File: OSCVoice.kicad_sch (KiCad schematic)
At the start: 38 parts, among them U10 TL074, U9 SSI2131

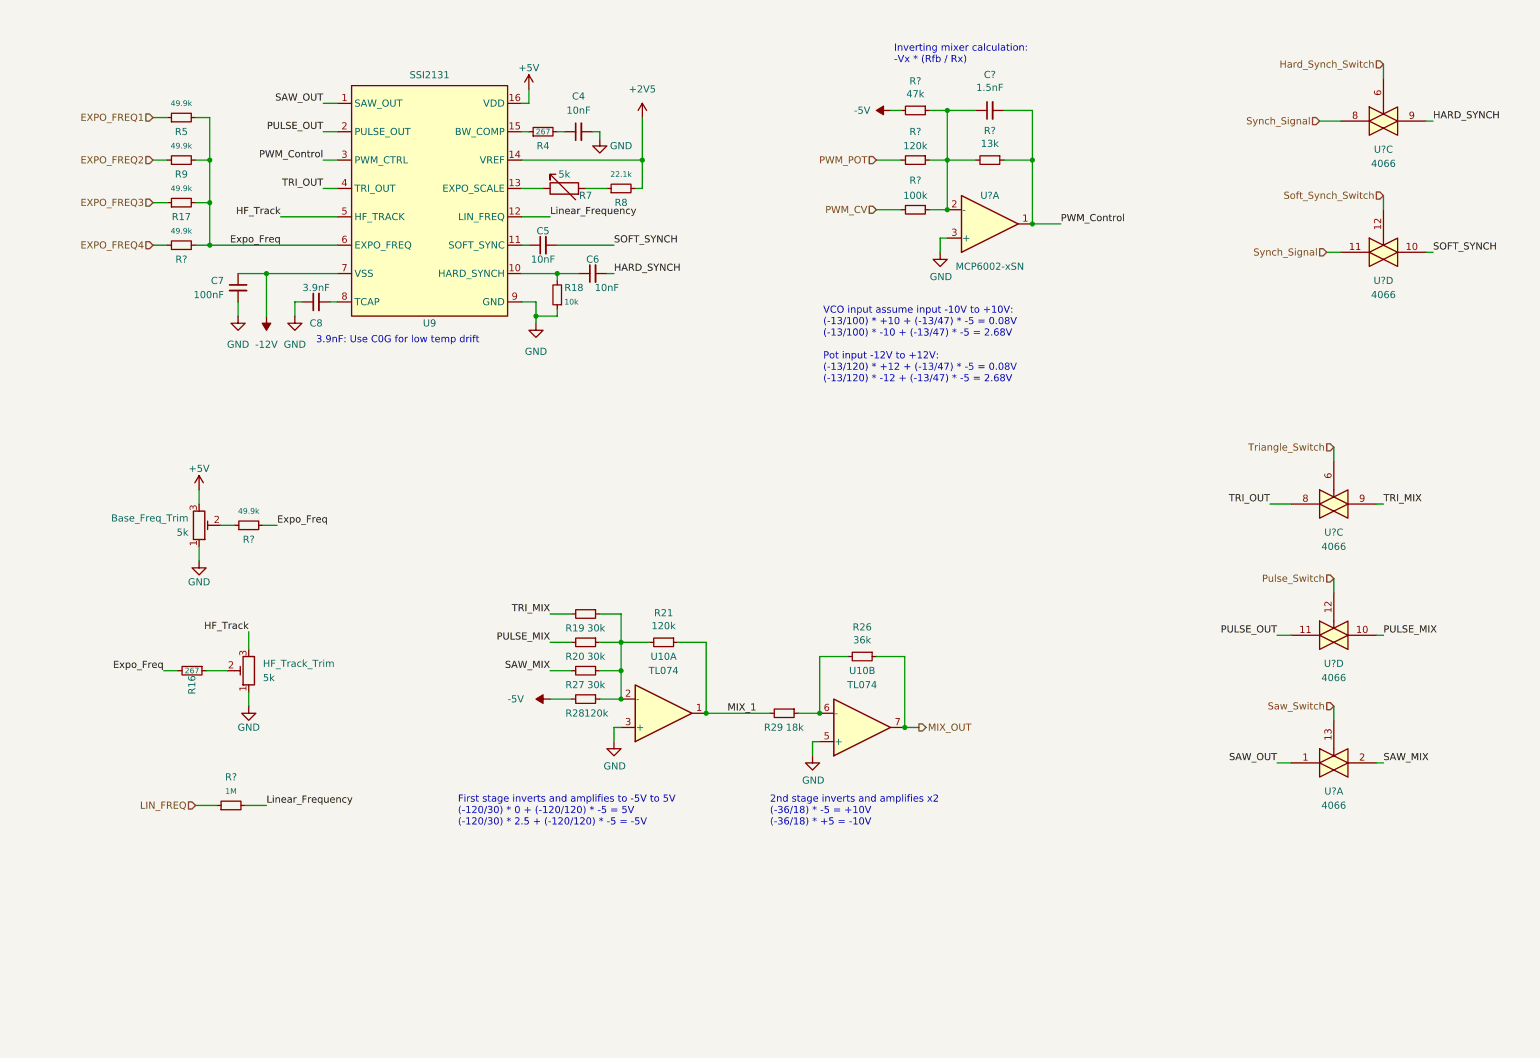
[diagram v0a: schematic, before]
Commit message: Split components and control pcbs
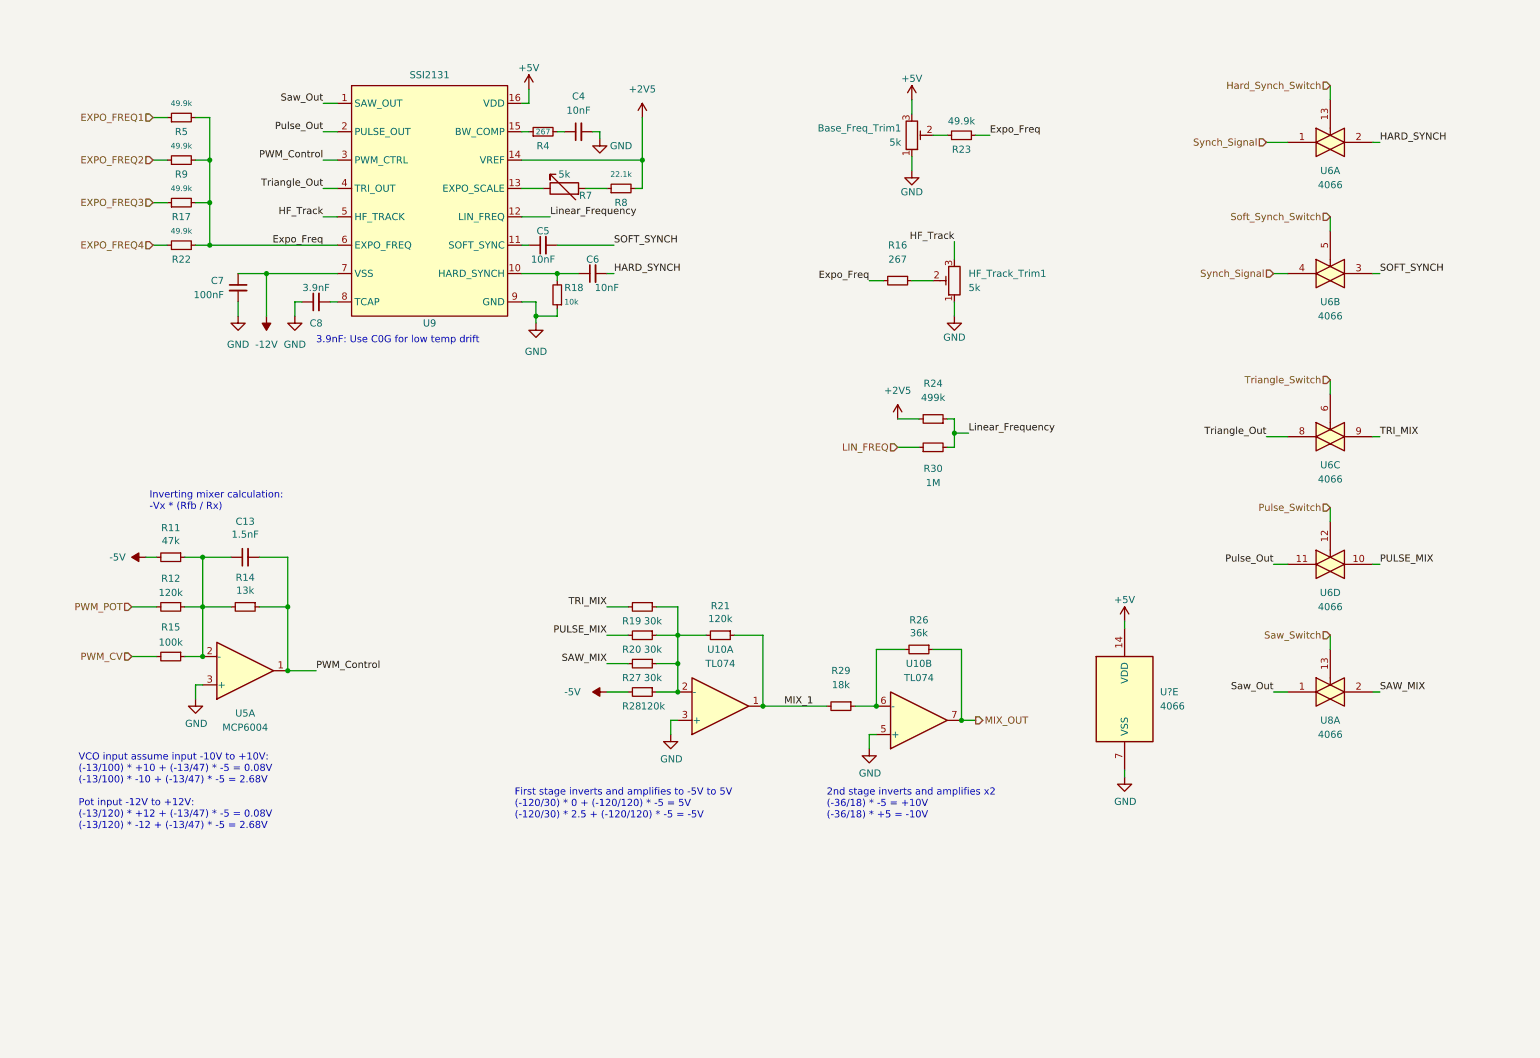
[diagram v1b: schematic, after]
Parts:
- removed U?: MCP6002-xSN, Package_SO:MSOP-8_3x3mm_P0.65mm, symbol Amplifier_Operational:MCP6002-xSN
- added R24: 499k, Resistor_SMD:R_0603_1608Metric, symbol Device:R_Small
- added U5: MCP6004, Package_SO:SOIC-14_3.9x8.7mm_P1.27mm, symbol Amplifier_Operational:MCP6004
- added U?: 4066, Package_SO:TSSOP-14_4.4x5mm_P0.65mm, symbol 4xxx:4066
- C4, C5, C6, C7: footprint Capacitor_SMD:C_0805_2012Metric -> Capacitor_SMD:C_0603_1608Metric_Pad1.08x0.95mm_HandSolder
- R11, R12, R14, R15, R22, R23, R30: renamed from R?; footprint Resistor_SMD:R_0805_2012Metric -> Resistor_SMD:R_0603_1608Metric
- R16, R17, R18, R19, R20, R21, R26, R27, R28, R29, R4, R5, R8, R9: footprint Resistor_SMD:R_0805_2012Metric -> Resistor_SMD:R_0603_1608Metric
- U10: footprint (none) -> Package_SO:SOIC-14_3.9x8.7mm_P1.27mm
- gave numbers to parts that had none: 3
- renumbered Base_Freq_Trim to Base_Freq_Trim1, HF_Track_Trim to HF_Track_Trim1
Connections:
- net +2V5: now also R24.2
- net +5V: now also U?.14 (VDD)
- net GND: now also U5.3 (+), U?.7 (VSS)
- net HARD_SYNCH: now also U6.2; no longer U6.9
- net Hard_Synch_Switch: now also U6.13; no longer U6.6
- net Linear_Frequency: now also R24.1
- net PWM_Control: now also U5.1
- net SOFT_SYNCH: now also U6.3; no longer U6.10
- net Soft_Synch_Switch: now also U6.5; no longer U6.12
- net Synch_Signal: now also U6.1, U6.4; no longer U6.11, U6.8
- net at C13.1, R11.1, R12.1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: now also U5.2 (-)
- net PULSE_OUT renamed Pulse_Out
- net SAW_OUT renamed Saw_Out
- net TRI_OUT renamed Triangle_Out
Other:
- moved on the sheet: Base_Freq_Trim1, C13, HF_Track_Trim1, R11, R12, R14, R15, R16, R19, R20, R21, R23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

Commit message: Started PCB layout
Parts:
- added R25: 100k, Resistor_SMD:R_0603_1608Metric, symbol Device:R_Small
- gave numbers to parts that had none: 1
- renumbered R7 to Expo_Trim1
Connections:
- net PWM_CV: now also R25.2; no longer R15.2
- net at C13.1, R11.1, R12.1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: now also R25.1
- net PULSE_MIX renamed Pulse_Mix
- net SAW_MIX renamed Saw_Mix
- net TRI_MIX renamed Triangle_Mix
- new net PWM_CV_ALL: R15.2
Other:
- moved on the sheet: R11, R12

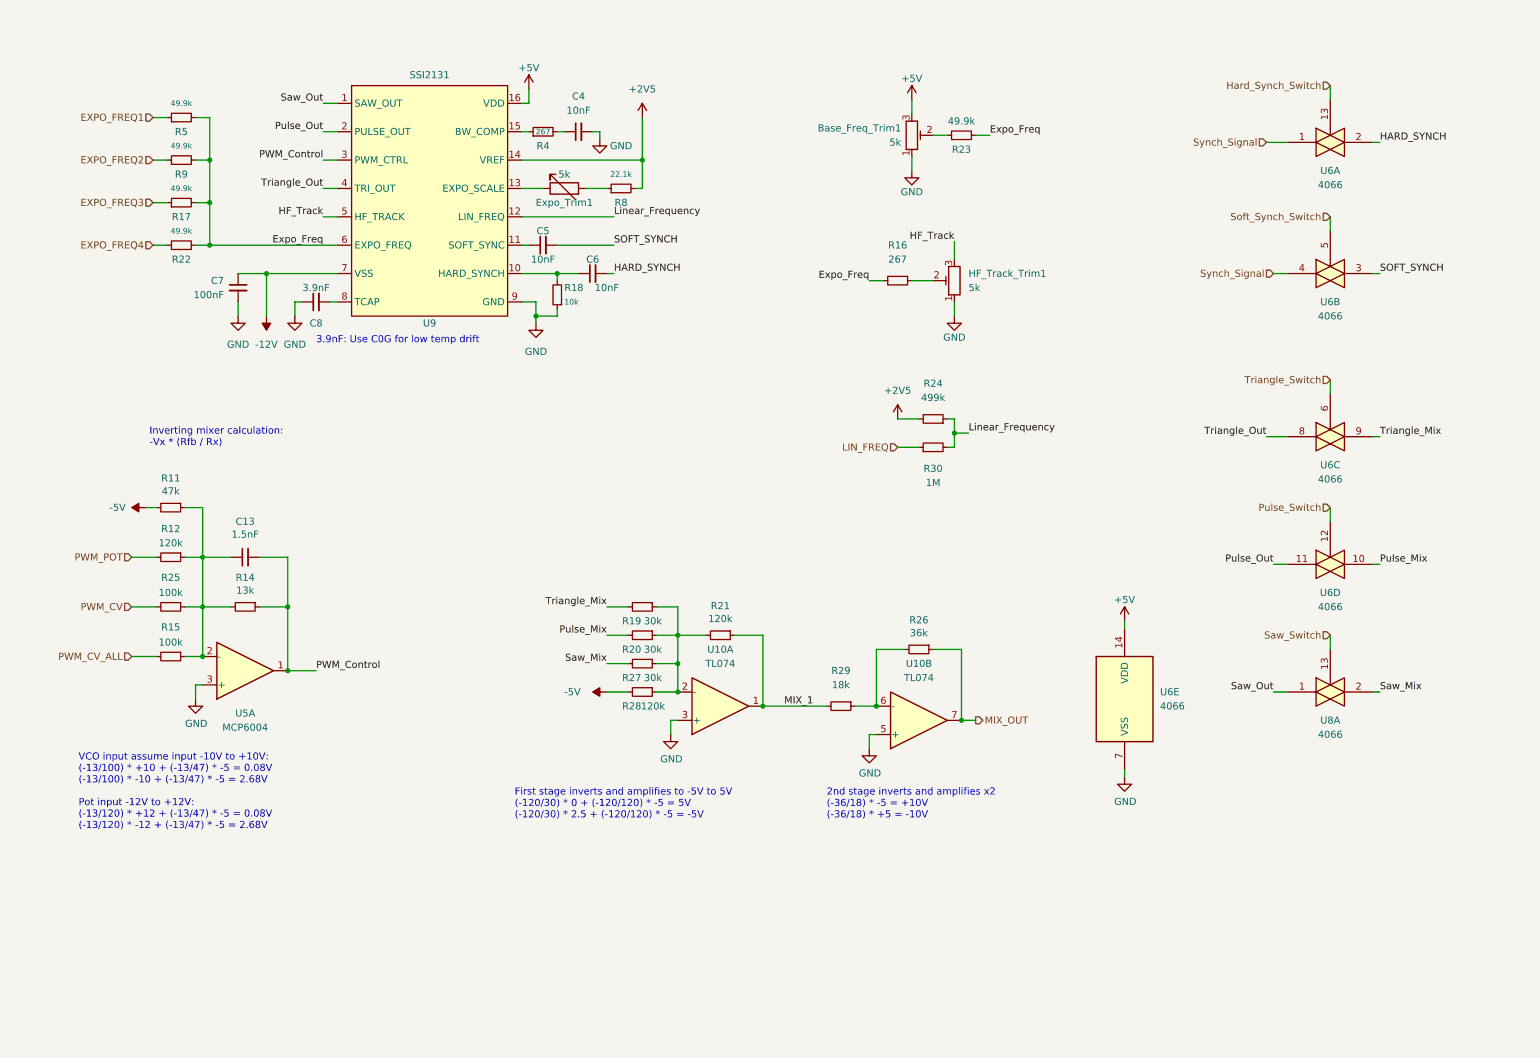
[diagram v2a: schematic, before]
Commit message: Updated design to use buffered 2.5V reference
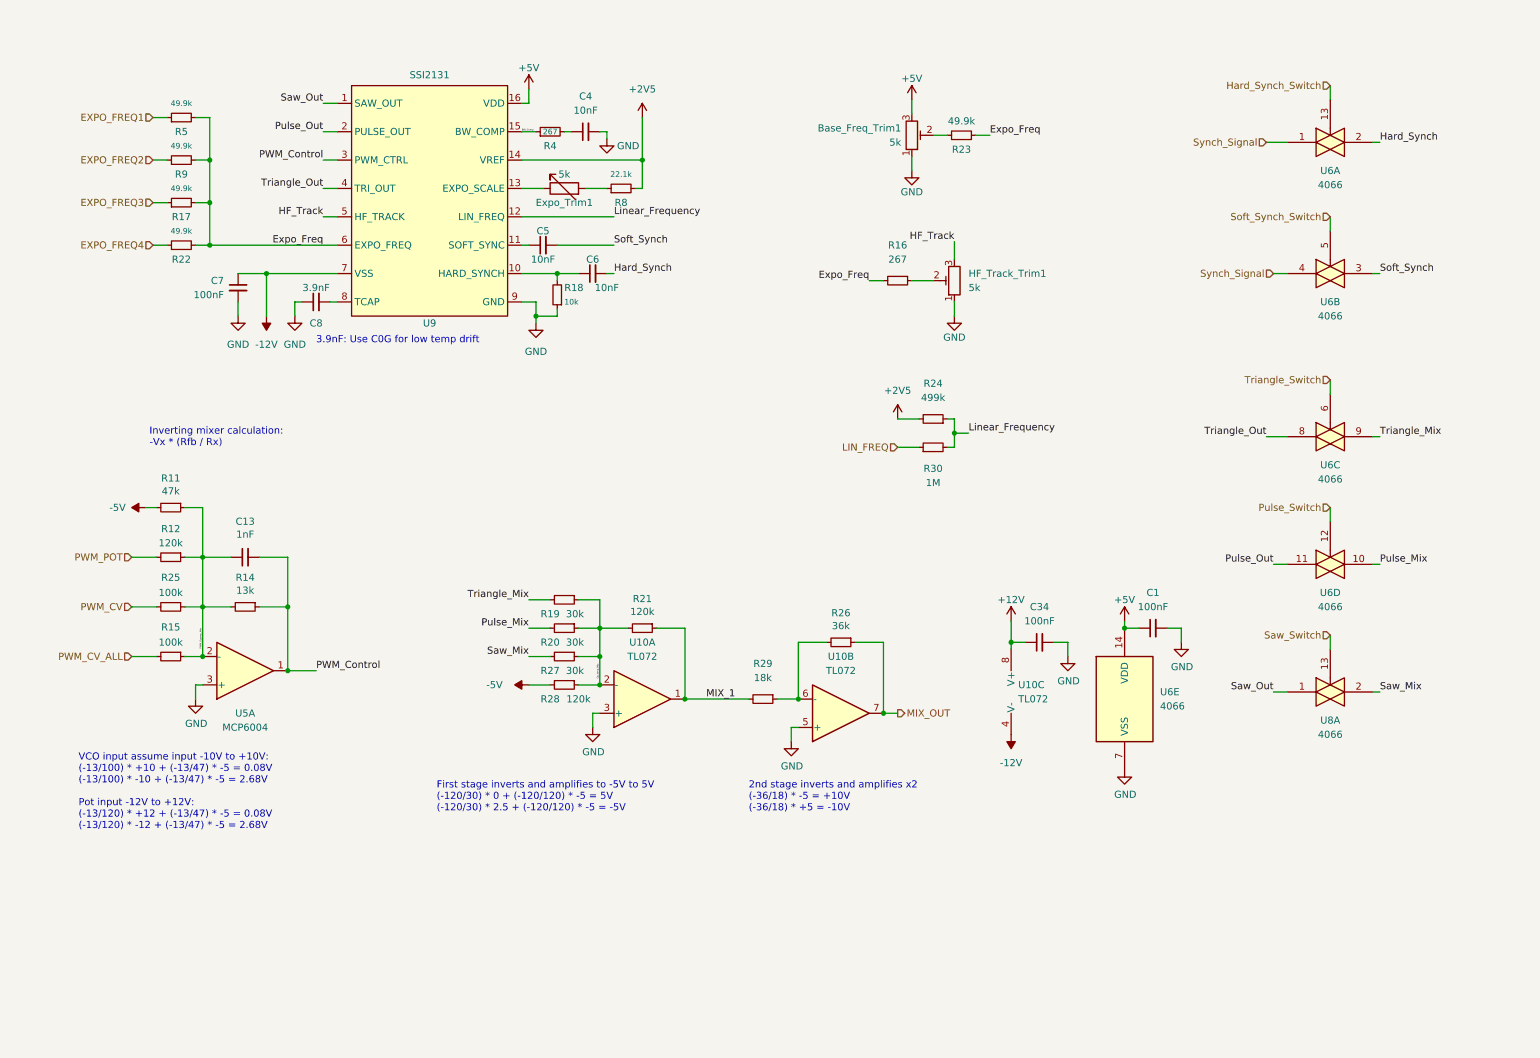
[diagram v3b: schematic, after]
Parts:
- removed U10: TL074, Package_SO:SOIC-14_3.9x8.7mm_P1.27mm, symbol Amplifier_Operational:TL074
- added C1, C34: 100nF, Capacitor_SMD:C_0603_1608Metric_Pad1.08x0.95mm_HandSolder, symbol Device:C_Small
- added U10: TL072, Package_SO:SOIC-8_3.9x4.9mm_P1.27mm, symbol Amplifier_Operational:TL072
- C13: value 1.5nF -> 1nF; footprint Capacitor_SMD:C_0805_2012Metric -> Capacitor_SMD:C_0603_1608Metric_Pad1.08x0.95mm_HandSolder
- C8: footprint Capacitor_SMD:C_0805_2012Metric -> Capacitor_SMD:C_0603_1608Metric_Pad1.08x0.95mm_HandSolder
- Expo_Trim1: footprint Potentiometer_THT:Potentiometer_Piher_PT-6-V_Vertical -> Potentiometer_THT:Potentiometer_Bourns_3266W_Vertical
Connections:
- net +5V: now also C1.1
- net -12V: now also U10.4 (V-)
- net GND: now also C1.2, C34.2, U10.3 (+), U10.5 (+)
- net MIX_1: now also U10.1
- net MIX_OUT: now also U10.7
- net PWM_Opamp_Mix: now reaches C13.1, R11.1, R12.1, R14.2, R15.1, R25.1, U5.2 (-)
- net Op_Amp_Mix: now reaches R19.1, R20.1, R21.2, R27.1, R28.1
- net Op_Amp_Mix: now also U10.2 (-)
- net at R26.2, R29.1: now also U10.6 (-)
- net BW_Comp: now reaches R4.1, U9.15 (BW_COMP)
- net HARD_SYNCH renamed Hard_Synch
- net SOFT_SYNCH renamed Soft_Synch
- new net +12V: C34.1, U10.8 (V+)
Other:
- moved on the sheet: C4, R19, R20, R21, R26, R27, R28, R29, R4

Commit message: Rough layout of one voice
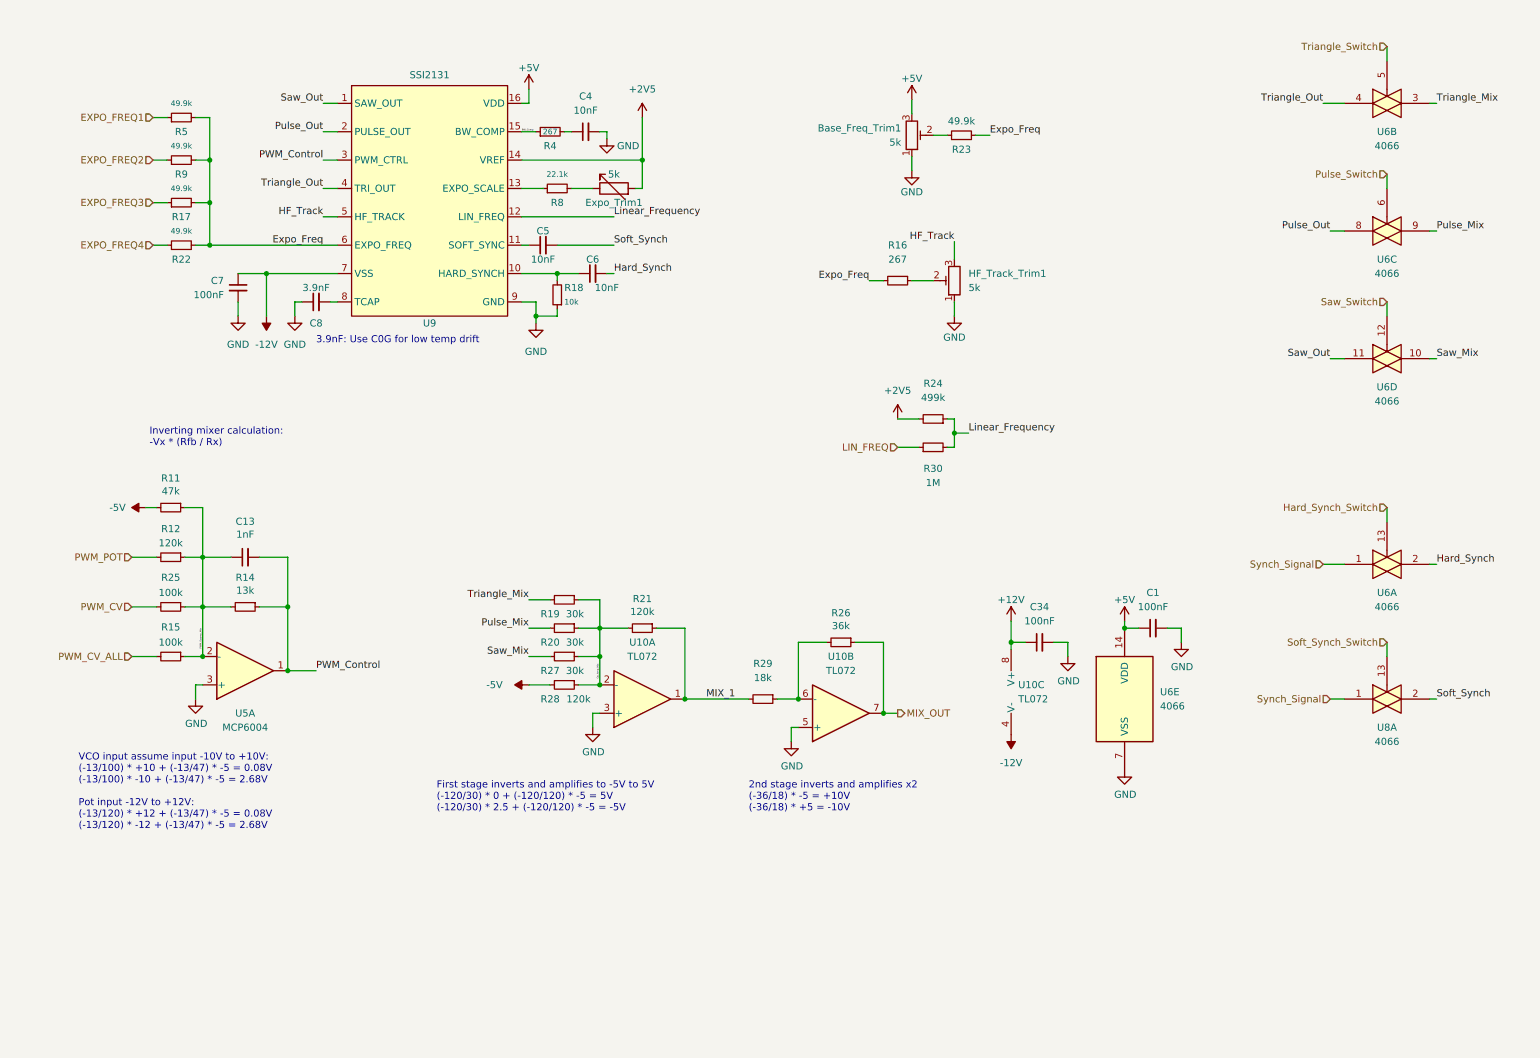
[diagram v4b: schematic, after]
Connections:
- net +2V5: now also Expo_Trim1.2; no longer R8.2
- net Hard_Synch: now also U6.2; no longer U6.2
- net Hard_Synch_Switch: now also U6.13; no longer U6.13
- net Pulse_Mix: now also U6.9; no longer U6.10
- net Pulse_Out: now also U6.8; no longer U6.11
- net Pulse_Switch: now also U6.6; no longer U6.12
- net Saw_Mix: now also U6.10; no longer U8.2
- net Saw_Out: now also U6.11; no longer U8.1
- net Saw_Switch: now also U6.12; no longer U8.13
- net Soft_Synch: now also U8.2; no longer U6.3
- net Soft_Synch_Switch: now also U8.13; no longer U6.5
- net Synch_Signal: now also U6.1, U8.1; no longer U6.1, U6.4
- net Triangle_Mix: now also U6.3; no longer U6.9
- net Triangle_Out: now also U6.4; no longer U6.8
- net Triangle_Switch: now also U6.5; no longer U6.6
- net at R8.1: now also U9.13 (EXPO_SCALE); no longer Expo_Trim1.2
- net at Expo_Trim1.1: now also R8.2; no longer U9.13 (EXPO_SCALE)
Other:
- moved on the sheet: Expo_Trim1, R8, U6A, U6B, U6C, U6D, U8A
